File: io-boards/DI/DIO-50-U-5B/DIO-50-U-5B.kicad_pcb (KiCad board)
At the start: 2 copper layers, 50 x 33 mm, 13 parts, among them J1 GPP_Conn_01x12_Pin, J2 Conn_01x03_Pin, J3 Conn_01x02_Socket, J4 Conn_01x02_Socket, U1 PC817

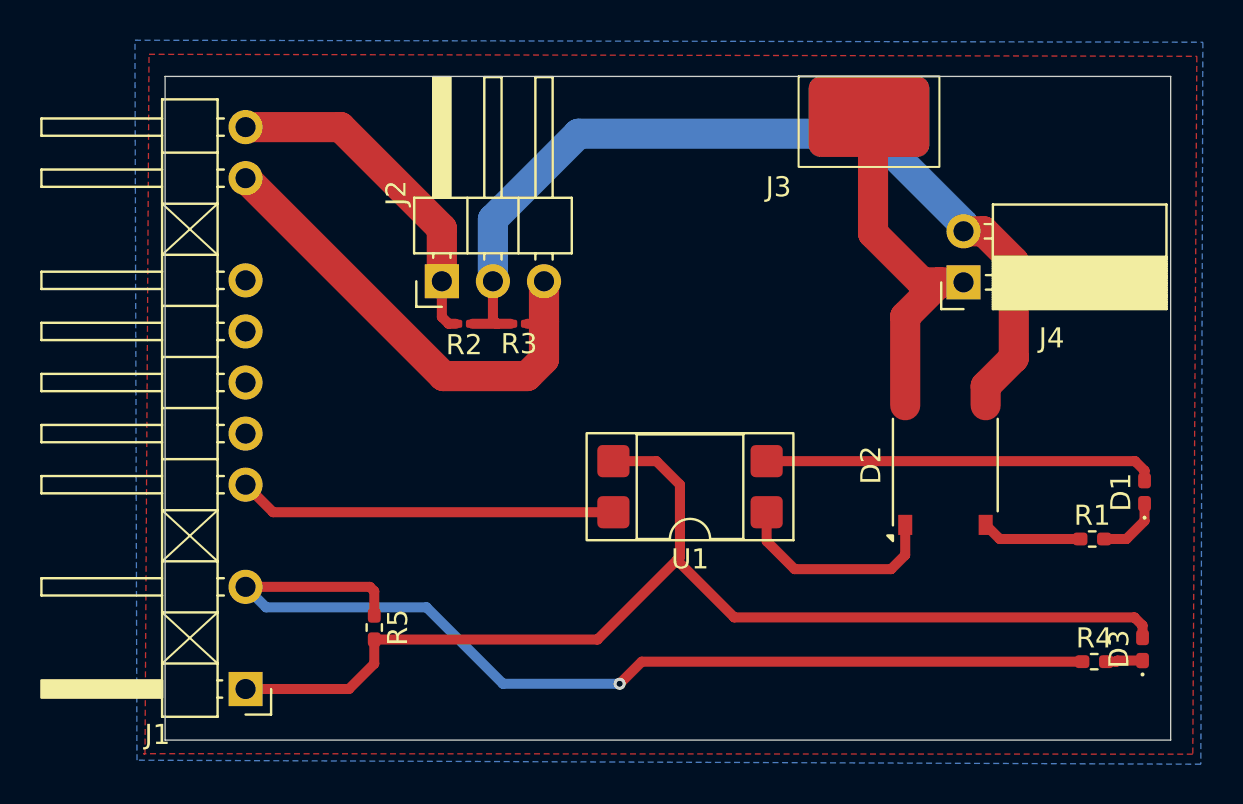
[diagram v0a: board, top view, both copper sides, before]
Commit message: Made some corrections after assembling of prototype PCBs
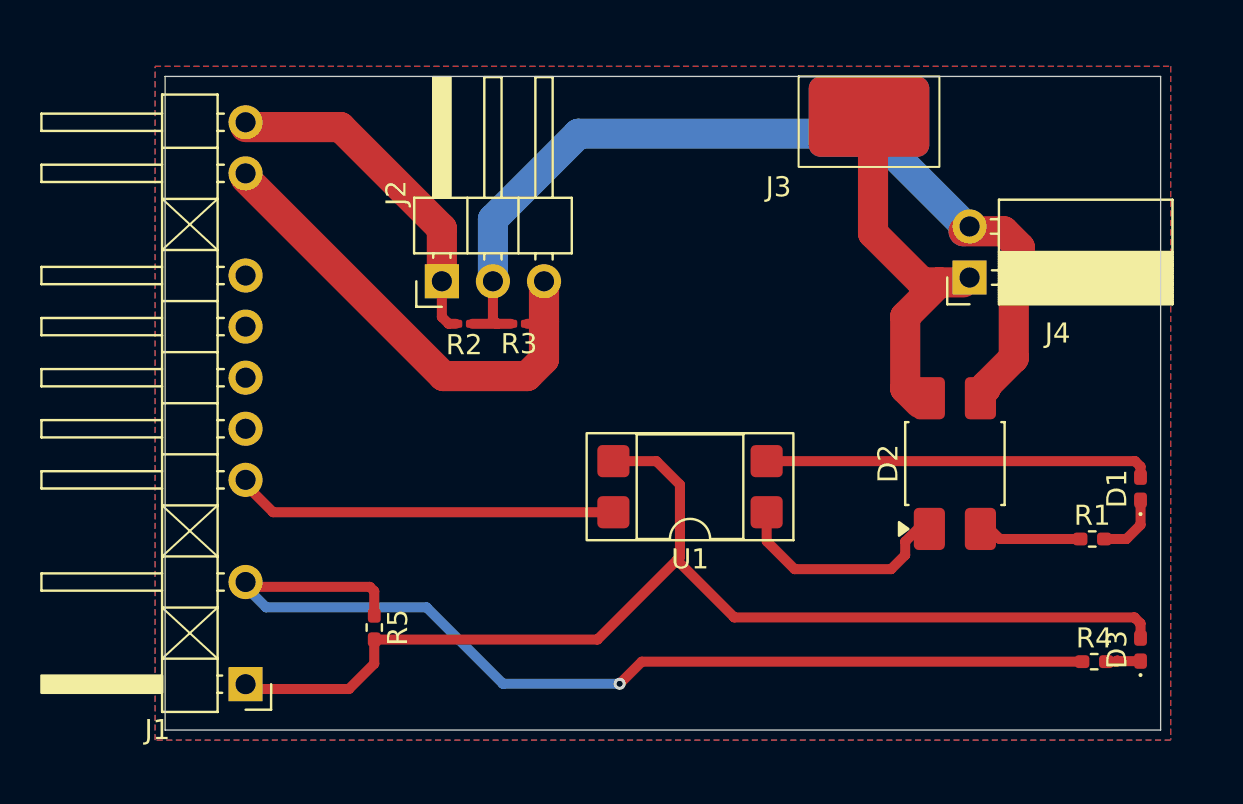
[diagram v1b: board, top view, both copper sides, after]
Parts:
- D2: value ABS2 -> MB8S; footprint Diode_SMD:Diode_Bridge_Diotec_ABS -> Package_SO:OnSemi_751EP_SOIC-4_3.9x4.725mm_P2.54mm
- moved D2 0.48 mm to (139.3, 69.2)
- moved J4 0.38 mm to (140.0, 60.0)
- moved D1 0.26 mm to (148.5, 70.5)
- moved J1 0.24 mm to (104.0, 80.2)
- moved D3 0.10 mm to (148.5, 78.5)
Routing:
- net Net-(D2--): track 4.99 -> 5.68 mm
- net Net-(J2-Pin_2): track 46.4 -> 47.0 mm
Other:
- board size 50 x 33 mm -> 49.5 x 32.5 mm
